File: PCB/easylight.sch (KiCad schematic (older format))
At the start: 49 parts, among them J1 LiPo (1S/3.7V), J2 USB/PWR, J3 LEDs, J4 AVR-ISP, J5 SW1, J6 SW1, J7 SW1, Q1 AO3415_C181094, Q2 AO3415_C181094, SW0 SPEF110100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

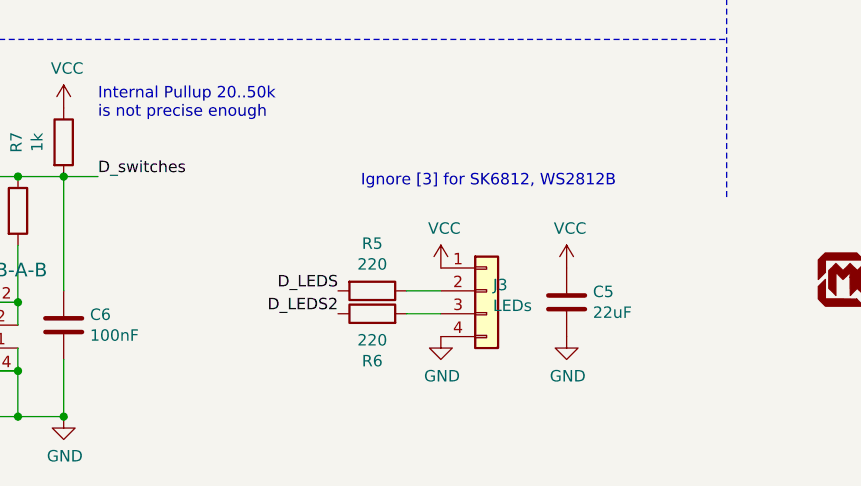
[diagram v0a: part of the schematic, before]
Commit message: add additional capacitor, make data resistors 470R, add template texts in preparation for KiCAD 6, extend readme
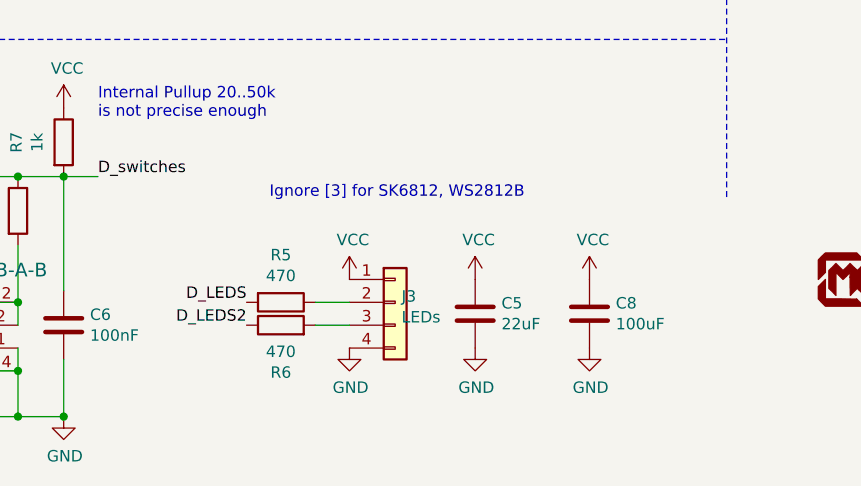
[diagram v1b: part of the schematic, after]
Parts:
- added C8: 100uF, Capacitor_SMD:C_1206_3216Metric_Pad1.42x1.75mm_HandSolder, symbol Device:C
- R5, R6: value 220 -> 470; LCSC Part C22962 -> C23179
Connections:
- net GND: now also C8.2
- net VCC: now also C8.1
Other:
- moved on the sheet: C5, J3, R5, R6
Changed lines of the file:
@@
 	1    0    0    -1
 $EndComp
-Text Label 5300 7000 2    50   ~ 0
+Text Label 4900 7050 2    50   ~ 0
 D_LEDS2
 $Comp
 L Connector_Generic:Conn_01x04 J3
 U 1 1 63F1784C
-P 5950 6900
-F 0 "J3" H 5978 6926 50  0000 L CNN
-F 1 "LEDs" H 5978 6835 50  0000 L CNN
-F 2 "Connector_JST:JST_XH_B4B-XH-A_1x04_P2.50mm_Vertical" H 5950 6900 50  0001 C CNN
-F 3 "~" H 5950 6900 50  0001 C CNN
-	1    5950 6900
+P 5550 6950
+F 0 "J3" H 5578 6976 50  0000 L CNN
+F 1 "LEDs" H 5578 6885 50  0000 L CNN
+F 2 "Connector_JST:JST_XH_B4B-XH-A_1x04_P2.50mm_Vertical" H 5550 6950 50  0001 C CNN
+F 3 "~" H 5550 6950 50  0001 C CNN
+	1    5550 6950
 	1    0    0    -1
 $EndComp
@@
 L power:VCC #PWR0107
 U 1 1 63F17852
-P 5750 6800
-F 0 "#PWR0107" H 5750 6650 50  0001 C CNN
-F 1 "VCC" H 5765 6973 50  0000 C CNN
-F 2 "" H 5750 6800 50  0001 C CNN
-F 3 "" H 5750 6800 50  0001 C CNN
-	1    5750 6800
+P 5350 6850
+F 0 "#PWR0107" H 5350 6700 50  0001 C CNN
+F 1 "VCC" H 5365 7023 50  0000 C CNN
+F 2 "" H 5350 6850 50  0001 C CNN
+F 3 "" H 5350 6850 50  0001 C CNN
+	1    5350 6850
 	1    0    0    -1
 $EndComp
@@
 L power:GND #PWR0108
 U 1 1 63F17858
-P 5750 7100
-F 0 "#PWR0108" H 5750 6850 50  0001 C CNN
-F 1 "GND" H 5755 6927 50  0000 C CNN
-F 2 "" H 5750 7100 50  0001 C CNN
-F 3 "" H 5750 7100 50  0001 C CNN
-	1    5750 7100
-	1    0    0    -1
-$EndComp
-Text Label 5300 6900 2    50   ~ 0
+P 5350 7150
+F 0 "#PWR0108" H 5350 6900 50  0001 C CNN
+F 1 "GND" H 5355 6977 50  0000 C CNN
+F 2 "" H 5350 7150 50  0001 C CNN
+F 3 "" H 5350 7150 50  0001 C CNN
+	1    5350 7150
+	1    0    0    -1
+$EndComp
+Text Label 4900 6950 2    50   ~ 0
 D_LEDS
-Text Notes 5400 6450 0    50   ~ 0
+Text Notes 5000 6500 0    50   ~ 0
 Ignore [3] for SK6812, WS2812B
 $Comp
@@
 L Device:C C5
 U 1 1 63FA7F7E
-P 6300 6950
-F 0 "C5" H 6415 6996 50  0000 L CNN
-F 1 "22uF" H 6415 6905 50  0000 L CNN
-F 2 "Capacitor_SMD:C_0603_1608Metric" H 6338 6800 50  0001 C CNN
-F 3 "~" H 6300 6950 50  0001 C CNN
-F 4 "C59461" H 6300 6950 50  0001 C CNN "LCSC Part"
-F 5 "Basic Part" H 6300 6950 50  0001 C CNN "JLC Part"
-	1    6300 6950
+P 5900 7000
+F 0 "C5" H 6015 7046 50  0000 L CNN
+F 1 "22uF" H 6015 6955 50  0000 L CNN
+F 2 "Capacitor_SMD:C_0603_1608Metric" H 5938 6850 50  0001 C CNN
+F 3 "~" H 5900 7000 50  0001 C CNN
+F 4 "C59461" H 5900 7000 50  0001 C CNN "LCSC Part"
+F 5 "Basic Part" H 5900 7000 50  0001 C CNN "JLC Part"
+	1    5900 7000
 	1    0    0    -1
 $EndComp
@@
 L power:VCC #PWR06
 U 1 1 63FA8BBB
-P 6300 6800
-F 0 "#PWR06" H 6300 6650 50  0001 C CNN
-F 1 "VCC" H 6315 6973 50  0000 C CNN
-F 2 "" H 6300 6800 50  0001 C CNN
-F 3 "" H 6300 6800 50  0001 C CNN
-	1    6300 6800
+P 5900 6850
+F 0 "#PWR06" H 5900 6700 50  0001 C CNN
+F 1 "VCC" H 5915 7023 50  0000 C CNN
+F 2 "" H 5900 6850 50  0001 C CNN
+F 3 "" H 5900 6850 50  0001 C CNN
+	1    5900 6850
 	1    0    0    -1
 $EndComp
@@
 L power:GND #PWR08
 U 1 1 63FA953E
-P 6300 7100
-F 0 "#PWR08" H 6300 6850 50  0001 C CNN
-F 1 "GND" H 6305 6927 50  0000 C CNN
-F 2 "" H 6300 7100 50  0001 C CNN
-F 3 "" H 6300 7100 50  0001 C CNN
-	1    6300 7100
+P 5900 7150
+F 0 "#PWR08" H 5900 6900 50  0001 C CNN
+F 1 "GND" H 5905 6977 50  0000 C CNN
+F 2 "" H 5900 7150 50  0001 C CNN
+F 3 "" H 5900 7150 50  0001 C CNN
+	1    5900 7150
 	1    0    0    -1
 $EndComp
@@
 L Device:R R5
 U 1 1 640610A3
-P 5450 6900
-F 0 "R5" V 5243 6900 50  0000 C CNN
-F 1 "220" V 5334 6900 50  0000 C CNN
-F 2 "Resistor_SMD:R_0603_1608Metric_Pad1.05x0.95mm_HandSolder" V 5380 6900 50  0001 C CNN
-F 3 "~" H 5450 6900 50  0001 C CNN
-F 4 "C22962" H 5450 6900 50  0001 C CNN "LCSC Part"
-F 5 "Basic Part" H 5450 6900 50  0001 C CNN "JLC Part"
-	1    5450 6900
+P 5050 6950
+F 0 "R5" V 4843 6950 50  0000 C CNN
+F 1 "470" V 4934 6950 50  0000 C CNN
+F 2 "Resistor_SMD:R_0603_1608Metric_Pad1.05x0.95mm_HandSolder" V 4980 6950 50  0001 C CNN
+F 3 "~" H 5050 6950 50  0001 C CNN
+F 4 "C23179" H 5050 6950 50  0001 C CNN "LCSC Part"
+F 5 "Basic Part" H 5050 6950 50  0001 C CNN "JLC Part"
+	1    5050 6950
 	0    1    1    0
 $EndComp
@@
 L Device:R R6
 U 1 1 64074821
-P 5450 7000
-F 0 "R6" V 5243 7000 50  0000 C CNN
-F 1 "220" V 5334 7000 50  0000 C CNN
-F 2 "Resistor_SMD:R_0603_1608Metric_Pad1.05x0.95mm_HandSolder" V 5380 7000 50  0001 C CNN
-F 3 "~" H 5450 7000 50  0001 C CNN
-F 4 "C22962" H 5450 7000 50  0001 C CNN "LCSC Part"
-F 5 "Basic Part" H 5450 7000 50  0001 C CNN "JLC Part"
-	1    5450 7000
+P 5050 7050
+F 0 "R6" V 4843 7050 50  0000 C CNN
+F 1 "470" V 4934 7050 50  0000 C CNN
+F 2 "Resistor_SMD:R_0603_1608Metric_Pad1.05x0.95mm_HandSolder" V 4980 7050 50  0001 C CNN
+F 3 "~" H 5050 7050 50  0001 C CNN
+F 4 "C23179" H 5050 7050 50  0001 C CNN "LCSC Part"
+F 5 "Basic Part" H 5050 7050 50  0001 C CNN "JLC Part"
+	1    5050 7050
 	0    -1   -1   0
 $EndComp
 Wire Wire Line
-	5600 7000 5750 7000
-Wire Wire Line
-	5600 6900 5750 6900
+	5200 7050 5350 7050
+Wire Wire Line
+	5200 6950 5350 6950
 $Comp
 L Device:R R7
@@
 	1    0    0    -1
 $EndComp
+$Comp
+L Device:C C8
+U 1 1 63D092DB
+P 6400 7000
+F 0 "C8" H 6515 7046 50  0000 L CNN
+F 1 "100uF" H 6515 6955 50  0000 L CNN
+F 2 "Capacitor_SMD:C_1206_3216Metric_Pad1.42x1.75mm_HandSolder" H 6438 6850 50  0001 C CNN
+F 3 "~" H 6400 7000 50  0001 C CNN
+F 4 "C15008" H 6400 7000 50  0001 C CNN "LCSC Part"
+F 5 "Basic Part" H 6400 7000 50  0001 C CNN "JLC Part"
+	1    6400 7000
+	1    0    0    -1
+$EndComp
+$Comp
+L power:VCC #PWR017
+U 1 1 63D092E1
+P 6400 6850
+F 0 "#PWR017" H 6400 6700 50  0001 C CNN
+F 1 "VCC" H 6415 7023 50  0000 C CNN
+F 2 "" H 6400 6850 50  0001 C CNN
+F 3 "" H 6400 6850 50  0001 C CNN
+	1    6400 6850
+	1    0    0    -1
+$EndComp
+$Comp
+L power:GND #PWR018
+U 1 1 63D092E7
+P 6400 7150
+F 0 "#PWR018" H 6400 6900 50  0001 C CNN
+F 1 "GND" H 6405 6977 50  0000 C CNN
+F 2 "" H 6400 7150 50  0001 C CNN
+F 3 "" H 6400 7150 50  0001 C CNN
+	1    6400 7150
+	1    0    0    -1
+$EndComp
